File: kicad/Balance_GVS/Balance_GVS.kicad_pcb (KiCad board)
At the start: 2 copper layers, 21.6 x 120.7 mm, 99 parts, among them J1 Conn_01x02_Pin, J10 I2C Header 2, J11 Conn_01x02_Pin, J12 Conn_01x02_Pin, J13 UART Header, J5 Conn_01x02_Pin, J6 Conn_01x03_Pin, J7 Conn_01x03_Pin, J8 Conn_01x05_Pin, J9 I2C Header 1, K1 AQY210S, Q3 2N3904, Q4 2N3904, SW2 EVQ-P7A01P, SW3 SW_Push, SW4 SW_Push, SW5 SW_Push, SW6 SW_Push, U1 ESP32-WROOM-32E, U10 INA219BxD, U11 LT1013DIP, U12 LT1013DIP, U3 OPA4313IPWR, U4 INA303A1IPW, U9 MCP4725xxx-xCH

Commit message: I kinda popped off ngl. Main pcb almost done
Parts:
- added H1: MountingHole, MountingHole:MountingHole_3.5mm, F.Cu at (88.2, 79.7)
- added H2: MountingHole, MountingHole:MountingHole_3.5mm, F.Cu at (123.5, 85.0)
- added J14: B3B-XH-A, B3B_XH_A:JST_B3B-XH-A, F.Cu at (88.3, 138.8)
- added J15: Conn_01x01_Pin, Connector_PinSocket_2.54mm:PinSocket_1x01_P2.54mm_Vertical, F.Cu at (86.5, 48.2)
- added J4: Conn_01x01_Pin, Connector_PinSocket_2.54mm:PinSocket_1x01_P2.54mm_Vertical, F.Cu at (133.2, 84.5)
- moved J5 193.7 mm to (85.8, 121.9)
- moved R27 170.5 mm to (93.2, 93.2), turned to 180 degrees
- moved R25 167.8 mm to (93.1, 97.7), turned to 0 degrees
- moved J11 165.0 mm to (85.8, 129.4), turned to 0 degrees
- moved U10 164.8 mm to (100.5, 96.1)
- moved R23 161.6 mm to (108.6, 93.0), turned to 0 degrees
- moved R31 160.6 mm to (99.7, 103.8), turned to -90 degrees
- moved R30 156.0 mm to (99.7, 109.1), turned to 90 degrees
- moved C15 154.8 mm to (116.1, 97.5), turned to 0 degrees
- moved R36 153.7 mm to (114.2, 132.0), turned to 0 degrees
- moved R37 152.1 mm to (114.1, 140.4)
- moved R35 150.1 mm to (115.2, 127.8), turned to 180 degrees
- moved R24 149.7 mm to (108.2, 79.5), turned to 90 degrees
- moved R6 148.7 mm to (87.4, 93.8), turned to -90 degrees
- moved C20 147.9 mm to (105.1, 109.1), turned to 90 degrees
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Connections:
- J7 pad 1: Net-(D10-A) -> Net-(D15-A)
- J7 pad 3: Net-(D15-A) -> Net-(D10-A)
- R2 pad 2: 1.65V -> VREF
- R3 pad 1: 1.65V -> VREF
- R49 pad 2: /Processor/Switch1 -> /Processor/Switch2
- R50 pad 2: /Processor/Switch2 -> /Processor/Switch1
- S1 pad 1A: /Processor/Switch1 -> /Processor/Switch2
- S1 pad 2A: /Processor/Switch2 -> /Processor/Switch1
- U3 pad 6: /Safety/VREF -> VREF
- U3 pad 7: /Safety/VREF -> VREF
- U4 pad 4: /Safety/VREF -> VREF
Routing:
- net GND: track 0.00 -> 132.7 mm, vias 0 -> 27
- net +3.3V: track 35.5 -> 126.9 mm, vias 0 -> 10
- net Battery_Voltage: track 41.7 -> 129.7 mm, vias 0 -> 1
- net DAC_OUT: track 3.62 -> 62.8 mm, vias 0 -> 2
- net VREF: track 0.00 -> 52.4 mm, vias 0 -> 2
- net Current_Sense-: track 39.8 -> 90.0 mm
- net /Processor/SCL1: track 34.3 -> 80.1 mm, vias 2 -> 1
- net /Safety/INP: track 18.2 -> 61.1 mm
- net Electrode+: track 41.7 -> 84.4 mm, vias 2 -> 3
- net /Processor/IO0: track 7.47 -> 37.4 mm, vias 0 -> 2
- net /Processor/SDA1: track 38.3 -> 67.7 mm, vias 0 -> 1
- net Safety-: track 42.7 -> 65.0 mm, vias 4 -> 2
- net Net-(D3-K): track 24.7 -> 46.2 mm
- net +24V: track 51.5 -> 71.9 mm, vias 2 -> 0
- net /Processor/TXD0: track 24.9 -> 5.91 mm, vias 2 -> 0
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- added copper zone on F.Cu, net +3.3V
- added copper zone on B.Cu, net GND
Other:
- board size 21.6 x 120.7 mm -> 53 x 96.9 mm

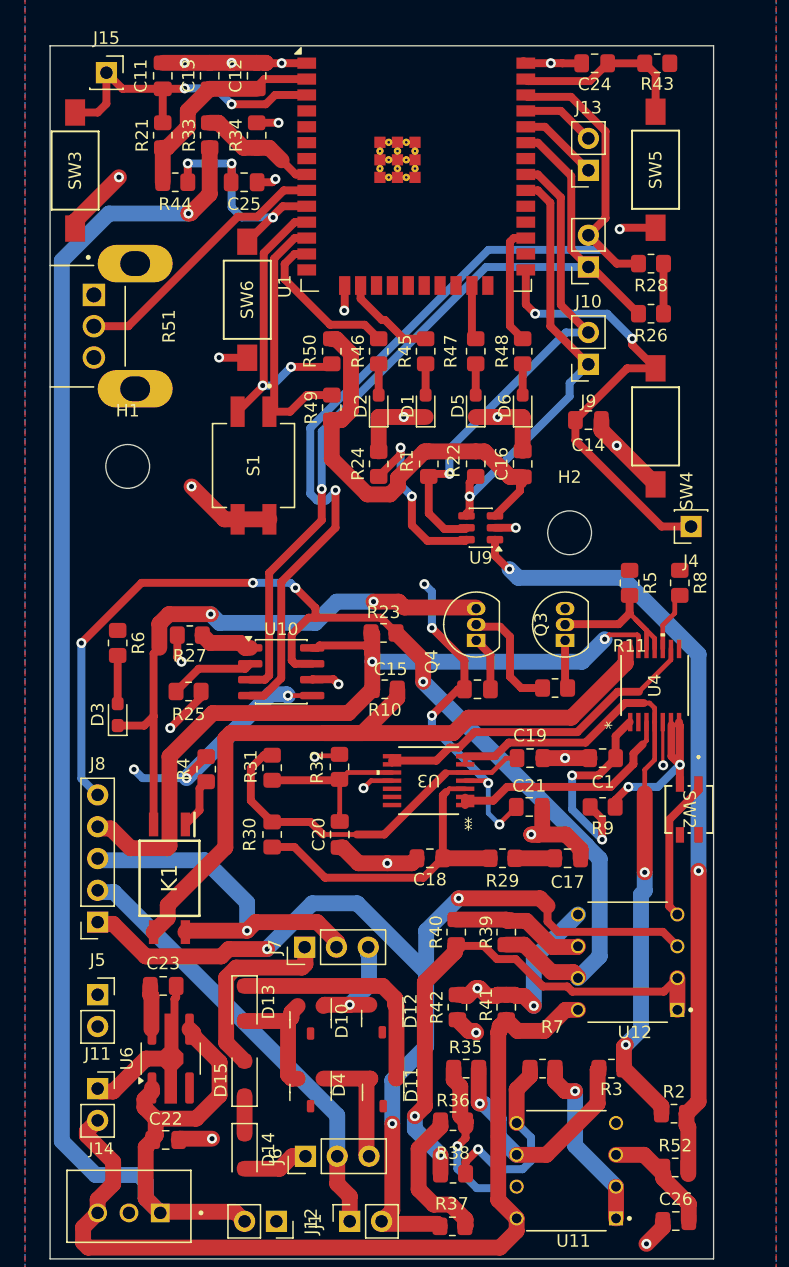
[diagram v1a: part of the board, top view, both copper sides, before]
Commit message: Add flip flop for better safety reset stability and remove NPNs
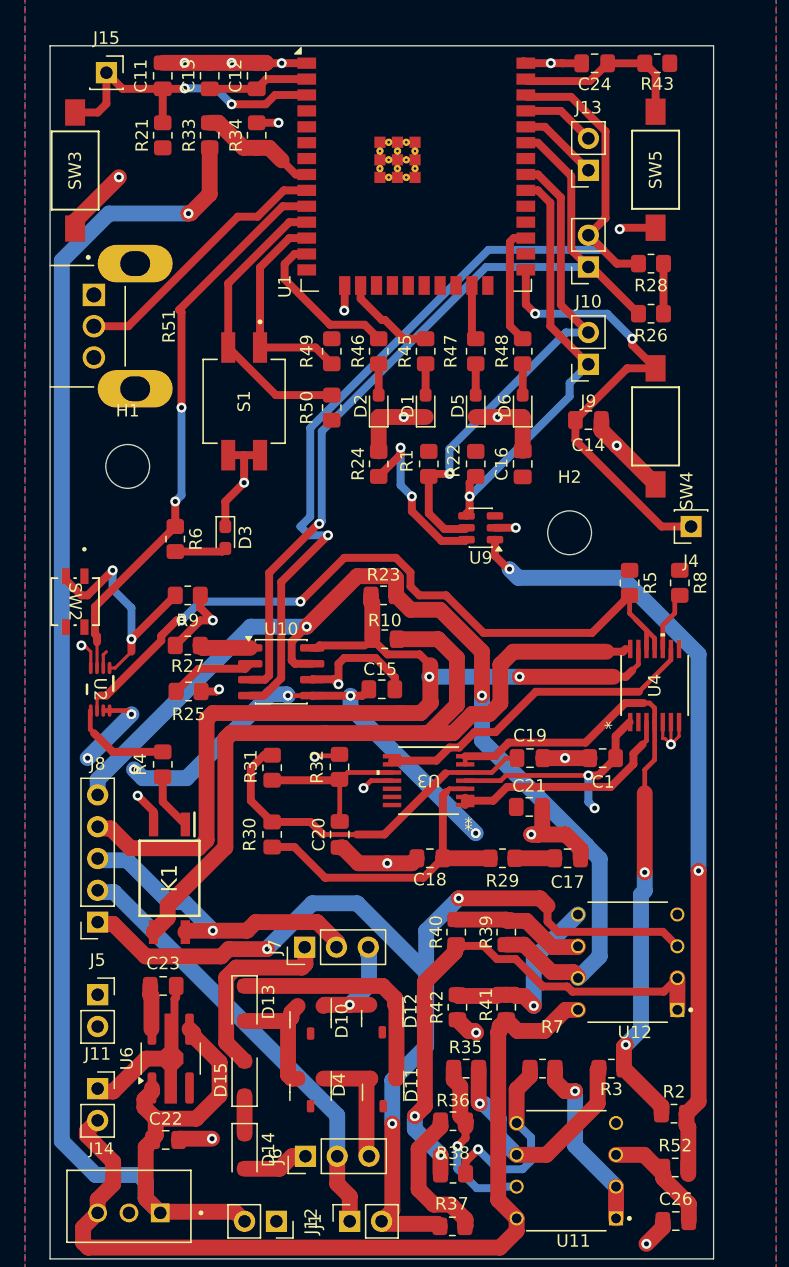
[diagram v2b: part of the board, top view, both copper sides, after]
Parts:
- removed C25: 0.1uF, Capacitor_SMD:C_0805_2012Metric_Pad1.18x1.45mm_HandSolder
- removed Q3, Q4: 2N3904, Package_TO_SOT_THT:TO-92_Inline
- removed R11: 3.3k, Resistor_SMD:R_0805_2012Metric_Pad1.20x1.40mm_HandSolder
- removed R44: 10K, Resistor_SMD:R_0805_2012Metric_Pad1.20x1.40mm_HandSolder
- removed SW6: SW_Push, FSMSMTR:SWITCH_FSMSMTR_TYC
- added U2: SN74LVC1G74DCUR, SN74LVC1G74DCUR:DCU0008A_M, F.Cu at (86.0, 97.5)
- R9: value 10k -> 10K
- moved SW2 51.8 mm to (84.0, 90.5)
- moved R9 37.2 mm to (93.0, 90.0)
- moved D3 16.6 mm to (96.0, 85.4), turned to -90 degrees
- moved R6 9.49 mm to (92.0, 85.5)
- moved C15 7.64 mm to (108.5, 97.5)
- moved S1 5.18 mm to (97.5, 74.5)
- moved R49 4.50 mm to (104.5, 70.5), turned to -90 degrees
- moved R50 4.50 mm to (104.5, 75.0), turned to 90 degrees
- moved R10 4.00 mm to (108.7, 93.5)
- moved R4 3.49 mm to (91.0, 103.5)
- moved R23 3.00 mm to (108.6, 90.0)
- moved R27 0.84 mm to (93.0, 94.0)
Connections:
- net 1.65V renamed /Safety/1.65V
- D3 pad 1: Net-(D3-K) -> GND
- K1 pad 2: Net-(D3-K) -> GND
- R4 pad 1: +3.3V -> /Safety/NOT_TRIPPED
- R6 pad 1: +3.3V -> TRIPPED
- R9 pad 1: +3.3V -> /Safety/ARM
- R9 pad 2: Net-(U4-LATCH1) -> GND
- SW2 pad 1: GND -> +3.3V
- SW2 pad 2: Net-(U4-LATCH1) -> /Safety/ARM
- U1 pad 10: /Processor/Button2 -> TRIPPED
- U4 pad 6: Net-(U4-LATCH1) -> GND
- U4 pad 7: Net-(U4-LATCH1) -> GND
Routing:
- net Net-(D3-K): track 46.2 -> 0.00 mm, vias 2 -> 0
- net TRIPPED: track 0.00 -> 45.7 mm, vias 0 -> 2
- net Net-(U2-CLR_N): track 14.9 -> 60.6 mm, vias 0 -> 2
- net +3.3V: track 126.9 -> 83.6 mm, vias 10 -> 8
- net /Safety/ARM: track 0.00 -> 19.7 mm, vias 0 -> 2
- net /Processor/Button2: track 19.6 -> 0.00 mm, vias 3 -> 0
- net Net-(U4-LATCH1): track 15.3 -> 0.00 mm, vias 2 -> 0
- net Net-(Q4-B): track 9.36 -> 0.00 mm
- net /Safety/NOT_TRIPPED: track 0.00 -> 8.04 mm
- net Safety-: track 65.0 -> 72.5 mm
- net /Safety/INP: track 61.1 -> 67.5 mm
- net Current_Sense-: track 90.0 -> 84.4 mm, vias 4 -> 2
- net Safety+: track 29.2 -> 25.1 mm
- net Net-(Q3-E): track 3.88 -> 0.00 mm
- net /Processor/Switch2: track 21.2 -> 17.4 mm
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
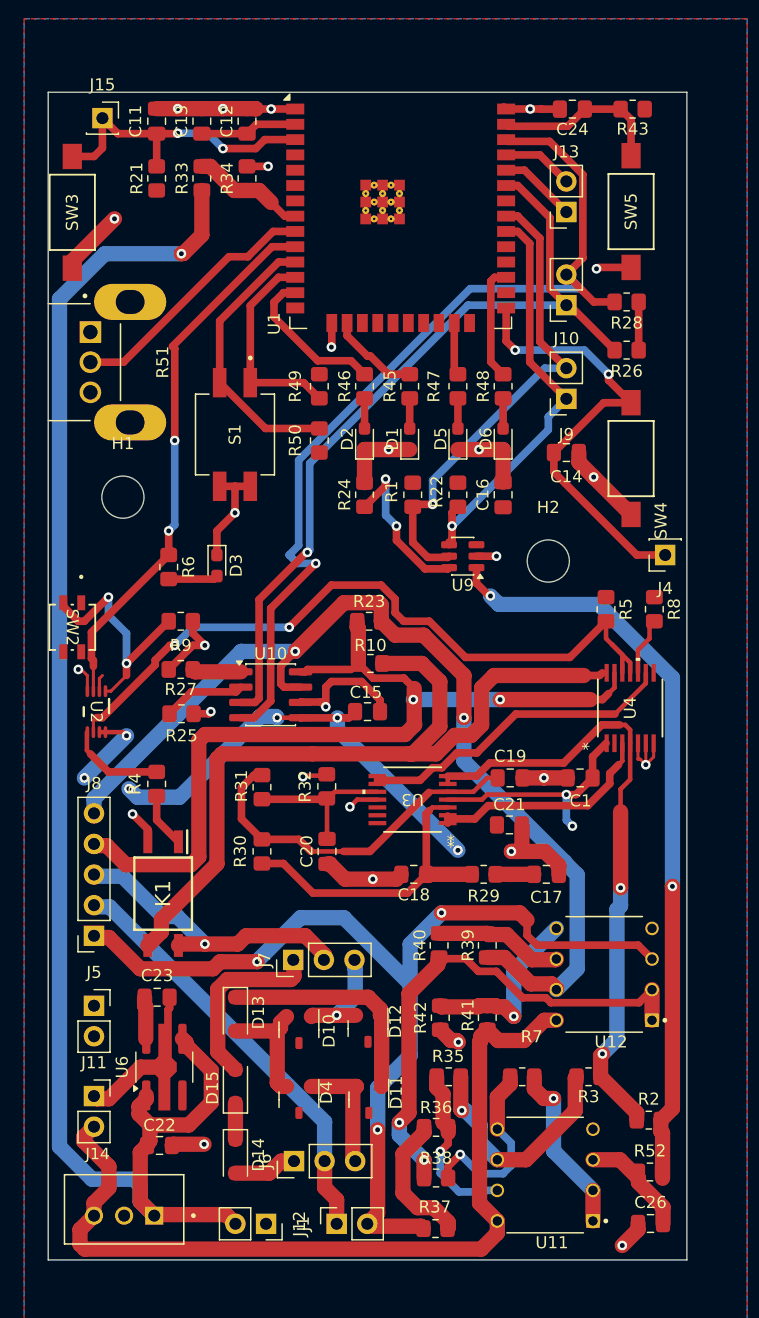
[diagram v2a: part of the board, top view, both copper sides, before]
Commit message: Add flip flop changes to PCB
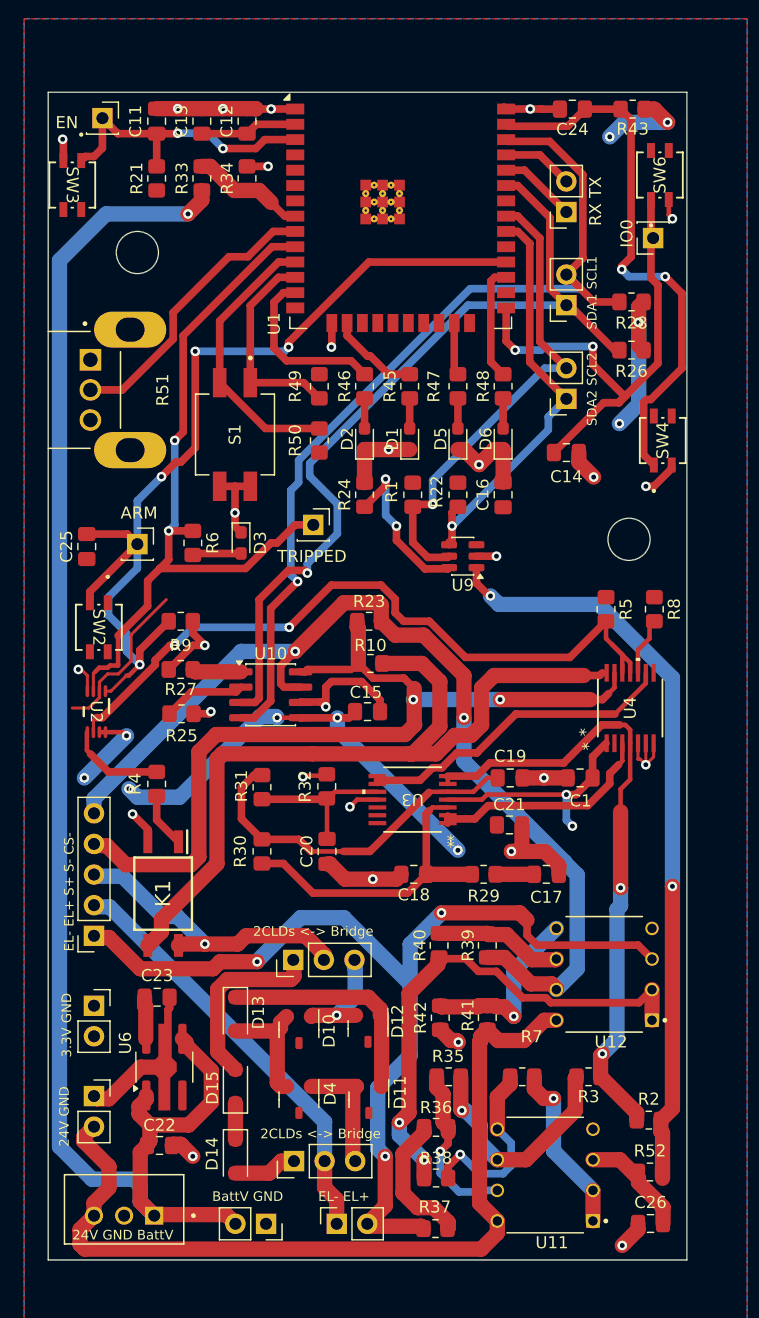
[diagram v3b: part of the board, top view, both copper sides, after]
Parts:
- removed SW5: SW_Push, FSMSMTR:SWITCH_FSMSMTR_TYC
- added C25: 0.1uF, Capacitor_SMD:C_0805_2012Metric_Pad1.18x1.45mm_HandSolder, F.Cu at (85.2, 83.8)
- added J16: Conn_01x01_Pin, Connector_PinSocket_2.54mm:PinSocket_1x01_P2.54mm_Vertical, F.Cu at (89.4, 83.6)
- added J17: Conn_01x01_Pin, Connector_PinSocket_2.54mm:PinSocket_1x01_P2.54mm_Vertical, F.Cu at (104.0, 82.0)
- added SW6: EVQ-P7A01P, EVQ_P7A01P:EVQ_P7_PAN, F.Cu at (132.8, 53.0)
- SW3, SW4: value SW_Push -> EVQ-P7A01P; footprint FSMSMTR:SWITCH_FSMSMTR_TYC -> EVQ_P7A01P:EVQ_P7_PAN
- moved J4 26.3 mm to (132.2, 58.2)
- moved H1 20.3 mm to (89.4, 59.4)
- moved H2 6.94 mm to (130.2, 83.2)
- moved SW3 6.90 mm to (84.0, 53.8), turned to -90 degrees
- moved SW4 6.68 mm to (133.0, 75.0)
- moved R6 2.83 mm to (94.0, 83.5)
- moved D3 2.74 mm to (98.0, 83.5)
- moved R51 2.30 mm to (85.5, 70.8)
- moved SW2 2.20 mm to (86.2, 90.5)
- moved R26 0.40 mm to (130.4, 67.5)
- moved R28 0.40 mm to (130.4, 63.5)
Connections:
- R9 pad 1: /Safety/ARM -> ARM
- SW2 pad 2: /Safety/ARM -> ARM
- SW3 pad 1: GND -> /Processor/EN
- SW3 pad 2: /Processor/EN -> GND
- SW4 pad 1: GND -> /Processor/Button1
- SW4 pad 2: /Processor/IO0 -> GND
- U1 pad 28: unconnected-(U1-IO17-Pad28) -> ARM
- U2 pad 1: /Safety/ARM -> ARM
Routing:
- net ARM: track 0.00 -> 78.8 mm, vias 0 -> 4
- net /Processor/Button1: track 14.4 -> 46.1 mm, vias 0 -> 2
- net +3.3V: track 83.6 -> 112.8 mm, vias 8 -> 12
- net /Safety/ARM: track 19.7 -> 0.00 mm, vias 2 -> 0
- net TRIPPED: track 45.7 -> 62.0 mm
- net GND: track 131.5 -> 123.6 mm, vias 27 -> 28
- net /Processor/IO0: track 37.4 -> 42.2 mm
- net /Processor/SDA1: track 67.8 -> 71.3 mm
- net /Processor/POT_ADC: track 21.5 -> 23.7 mm
- net /Processor/SCL1: track 79.0 -> 77.2 mm
- net /Processor/LED2: track 12.8 -> 14.3 mm
- net /Processor/EN: track 25.6 -> 25.0 mm
- net Safety-: track 72.5 -> 71.9 mm
- net Electrode+: track 84.4 -> 84.9 mm
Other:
- board text added: "24V GND"
- board text added: "24V GND BattV"
- board text added: "2CLDs <-> Bridge"
- board text added: "3.3V GND"
- board text added: "ARM"
- board text added: "BattV GND"
- board text added: "EL- EL+"
- board text added: "EL- EL+ S+ S- CS-"
- board text added: "EN"
- board text added: "IO0"
- board text added: "RX TX"
- board text added: "SDA1 SCL1"
- board text added: "SDA2 SCL2"
- board text added: "TRIPPED"

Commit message: Add Mark debug point testing and udpate silkscreen
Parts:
- removed J8: Conn_01x05_Pin, Connector_PinSocket_2.54mm:PinSocket_1x05_P2.54mm_Vertical
- added J18: Conn_01x03_Pin, Connector_PinHeader_2.54mm:PinHeader_1x03_P2.54mm_Vertical, F.Cu at (102.2, 131.2)
- added J19: Conn_01x03_Pin, Connector_PinHeader_2.54mm:PinHeader_1x03_P2.54mm_Vertical, F.Cu at (86.0, 111.5)
- added J2: Conn_01x01_Pin, Connector_PinSocket_2.54mm:PinSocket_1x01_P2.54mm_Vertical, F.Cu at (101.5, 126.5)
- added J20: Conn_01x03_Pin, Connector_PinHeader_2.54mm:PinHeader_1x03_P2.54mm_Vertical, F.Cu at (123.5, 89.0)
- added J21: Conn_01x01_Pin, Connector_PinSocket_2.54mm:PinSocket_1x01_P2.54mm_Vertical, F.Cu at (123.5, 84.5)
- added J22: Conn_01x01_Pin, Connector_PinSocket_2.54mm:PinSocket_1x01_P2.54mm_Vertical, F.Cu at (114.0, 91.5)
- added J3: Conn_01x01_Pin, Connector_PinSocket_2.54mm:PinSocket_1x01_P2.54mm_Vertical, F.Cu at (86.0, 106.5)
- moved D11 8.11 mm to (110.0, 120.5)
- moved D12 7.72 mm to (110.1, 115.0)
- moved J7 4.82 mm to (98.0, 116.0)
- moved D4 4.19 mm to (105.5, 124.8), turned to 0 degrees
- moved C12 4.00 mm to (94.5, 48.5)
- moved C13 3.75 mm to (98.5, 48.5)
- moved D10 3.30 mm to (104.0, 119.5)
- moved D13 1.10 mm to (97.5, 121.5)
- moved D15 1.10 mm to (97.5, 127.5)
- moved D14 0.90 mm to (97.5, 133.5)
- moved SW3 0.70 mm to (84.0, 54.5)
- moved R21 0.56 mm to (90.5, 53.5)
- moved J4 0.55 mm to (132.2, 58.8), turned to -90 degrees
- moved C11 0.50 mm to (90.5, 48.5)
- moved J1 0.50 mm to (105.9, 139.5)
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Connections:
- J6 pad 2: Electrode- -> Net-(J18-Pin_3)
- K1 pad 4: Safety+ -> Net-(J19-Pin_3)
- R23 pad 1: Safety- -> Net-(J20-Pin_3)
- U10 pad 8: Safety- -> Net-(J20-Pin_3)
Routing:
- net Safety-: track 71.9 -> 33.5 mm
- net Net-(J20-Pin_3): track 0.00 -> 32.8 mm, vias 0 -> 2
- net Electrode+: track 84.9 -> 53.3 mm, vias 3 -> 2
- net Current_Sense-: track 84.4 -> 61.4 mm, vias 2 -> 1
- net Electrode-: track 35.5 -> 15.9 mm
- net GND: track 123.6 -> 133.9 mm
- net Net-(D11-C): track 10.1 -> 19.4 mm
- net Safety+: track 25.1 -> 15.9 mm, vias 1 -> 0
- net Net-(J19-Pin_3): track 0.00 -> 8.17 mm
- net Net-(D10-C): track 10.2 -> 15.6 mm
- net /Safety/Electrode- TEST: track 0.00 -> 5.03 mm
- net /Safety/Safety+ TEST: track 0.00 -> 4.96 mm
- net Net-(J18-Pin_3): track 0.00 -> 4.79 mm
- net Net-(D10-A): track 8.97 -> 13.7 mm
- net /Processor/Safety- TEST: track 0.00 -> 4.46 mm
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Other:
- board text added: "Curr Sense-"
- board text added: "Elec-"
- board text added: "REG <-> TEST"
- board text added: "Safety+"
- board text added: "Safety-"
- board text removed: "EL- EL+ S+ S- CS-"

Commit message: Final Main PCB!
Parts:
- added C2: 100nF, Capacitor_SMD:C_0805_2012Metric_Pad1.18x1.45mm_HandSolder, F.Cu at (119.2, 125.2)
- added C3: 100nF, Capacitor_SMD:C_0805_2012Metric_Pad1.18x1.45mm_HandSolder, F.Cu at (115.2, 139.6)
- moved R37 2.47 mm to (111.8, 139.2), turned to 90 degrees
- moved R41 1.34 mm to (119.2, 121.8), turned to 0 degrees
- moved K1 1.20 mm to (91.5, 113.8)
- moved R3 1.16 mm to (128.0, 127.8)
- moved R7 0.80 mm to (121.3, 128.6)
- moved J1 0.74 mm to (105.2, 139.5)
- moved D15 0.54 mm to (97.0, 127.5)
- moved C26 0.52 mm to (132.5, 140.0)
- moved J7 0.50 mm to (98.0, 115.5)
- moved R2 0.41 mm to (132.2, 131.4)
- moved R38 0.40 mm to (114.2, 135.8)
- moved R52 0.31 mm to (132.2, 135.7)
- moved R42 0.30 mm to (114.5, 122.6)
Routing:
- net GND: track 133.9 -> 138.9 mm, vias 28 -> 30
- net Net-(R36-Pad1): track 11.3 -> 7.08 mm
- net +24V: track 71.8 -> 74.9 mm
- net /Processor/SCL1: track 77.2 -> 74.8 mm
- net Net-(K1-A): track 4.55 -> 5.75 mm
- net Net-(U11-2IN-): track 19.3 -> 20.5 mm
- net Electrode+: track 53.3 -> 52.2 mm
- net /HowlandPump/2IN+: track 15.8 -> 14.7 mm
- net /Processor/Button1: track 44.7 -> 45.7 mm
- net /HowlandPump/1IN-: track 14.5 -> 13.7 mm
- net Electrode-: track 15.9 -> 15.2 mm
- net Net-(D10-A): track 13.7 -> 14.4 mm
